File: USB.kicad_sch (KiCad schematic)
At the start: 46 parts, among them J3 USB_C_Receptacle_USB2.0, J4 USB_A_Stacked, U10 TPD4EUSB30, U4 CP2102N-Axx-xQFN20, U5 FSUSB42MUX, U6 FSUSB42MUX, U7 FE1.1, U8 TPD4EUSB30, U9 AP2191W, Y1 12MHz{slash}10pF

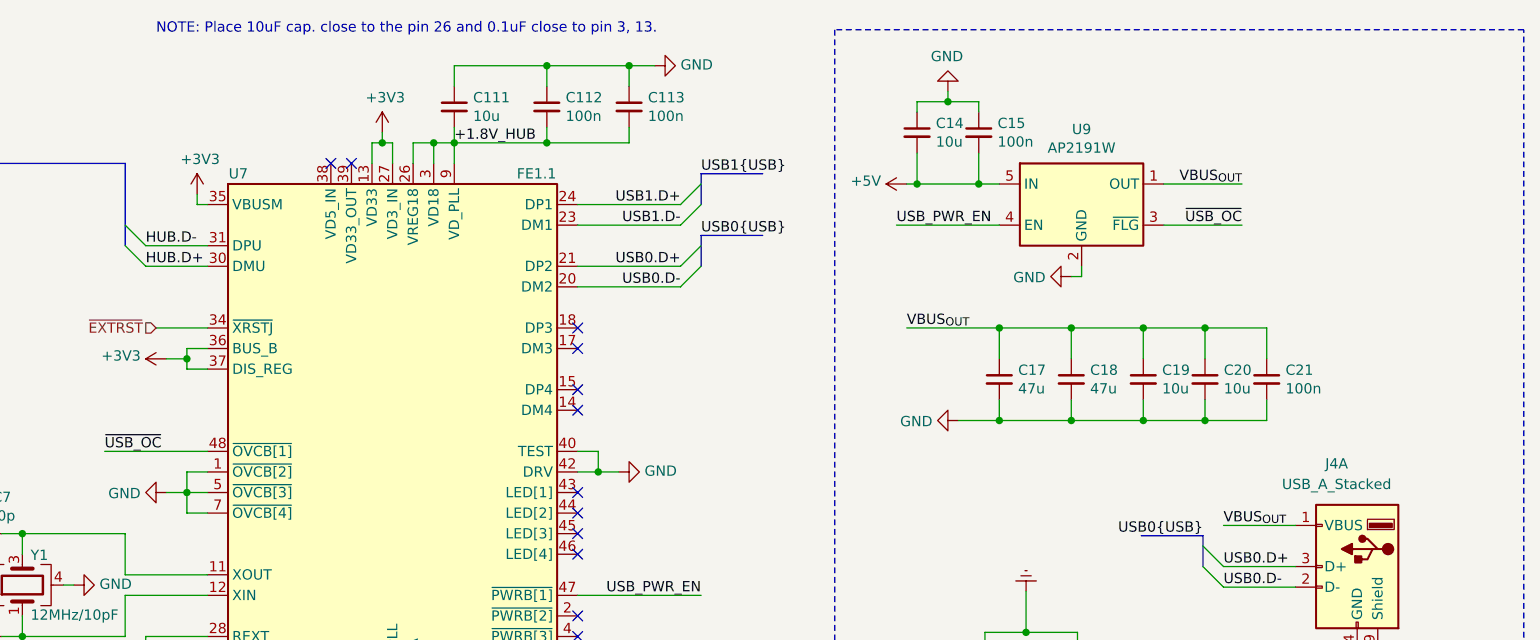
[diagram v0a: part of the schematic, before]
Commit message: USB hub fixes
-Fixed upstream diff pair polarity
-added optional inverer for the USB power switch enable pin
 Design now supports both AP2181 and AP2191

Signed-off-by: Dominik Sliwa <dominik@sliwa.io>
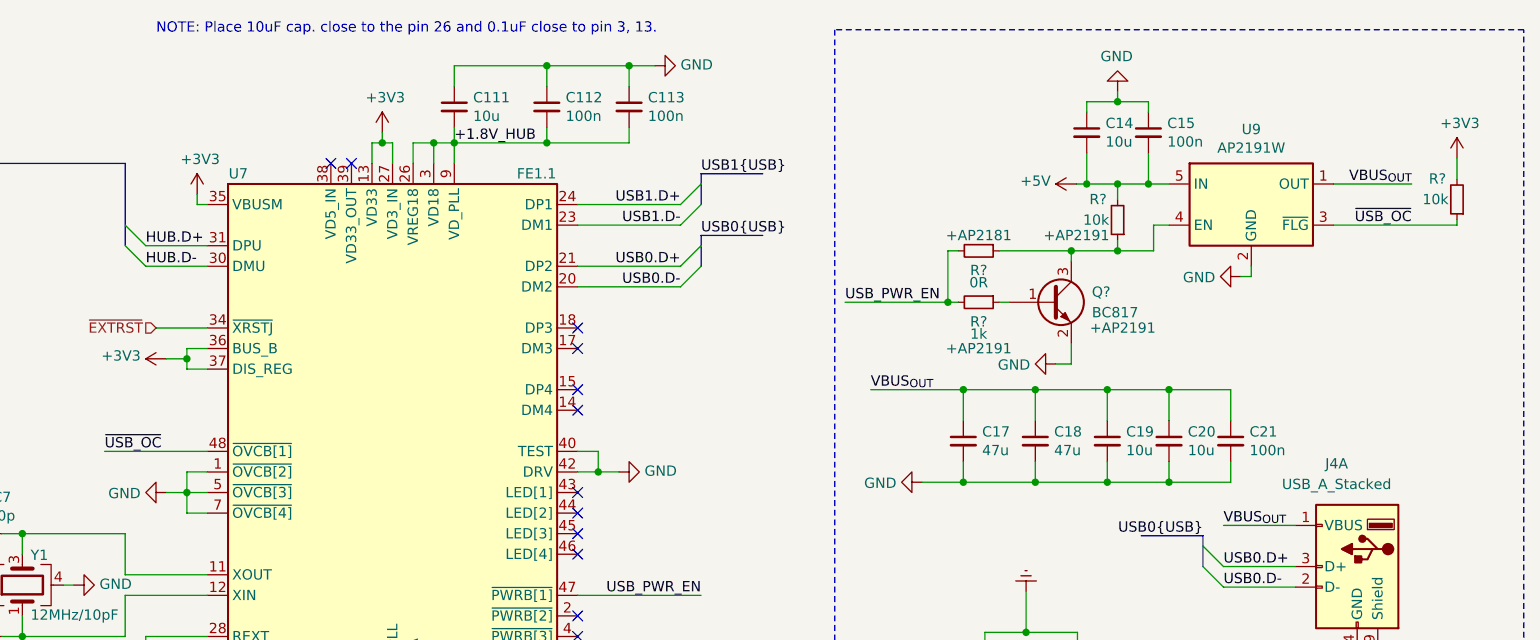
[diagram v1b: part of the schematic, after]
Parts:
- added Q?: BC817, Package_TO_SOT_SMD:SOT-23, symbol Transistor_BJT:BC817
- added R?: 1k, Resistor_SMD:R_0402_1005Metric, symbol Device:R_Small
- added R? (x2): 10k, Resistor_SMD:R_0402_1005Metric, symbol Device:R_Small
- added R?: 0R, Resistor_SMD:R_0402_1005Metric, symbol Device:R_Small
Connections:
- net +3V3: now also R?.2
- net +5V: now also R?.2
- net GND: now also Q?.2 (E)
- net HUB.D+: now also U7.31 (DPU); no longer U7.30 (DMU)
- net HUB.D-: now also U7.30 (DMU); no longer U7.31 (DPU)
- net USB_PWR_EN: now also R?.2, R?.2; no longer U9.4 (EN)
- net ~{USB_OC}: now also R?.1
- new net: Q?.1 (B), R?.1
- new net: Q?.3 (C), R?.1, R?.1, U9.4 (EN)
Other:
- moved on the sheet: C14, C15, C17, C18, C19, C20, C21, U9

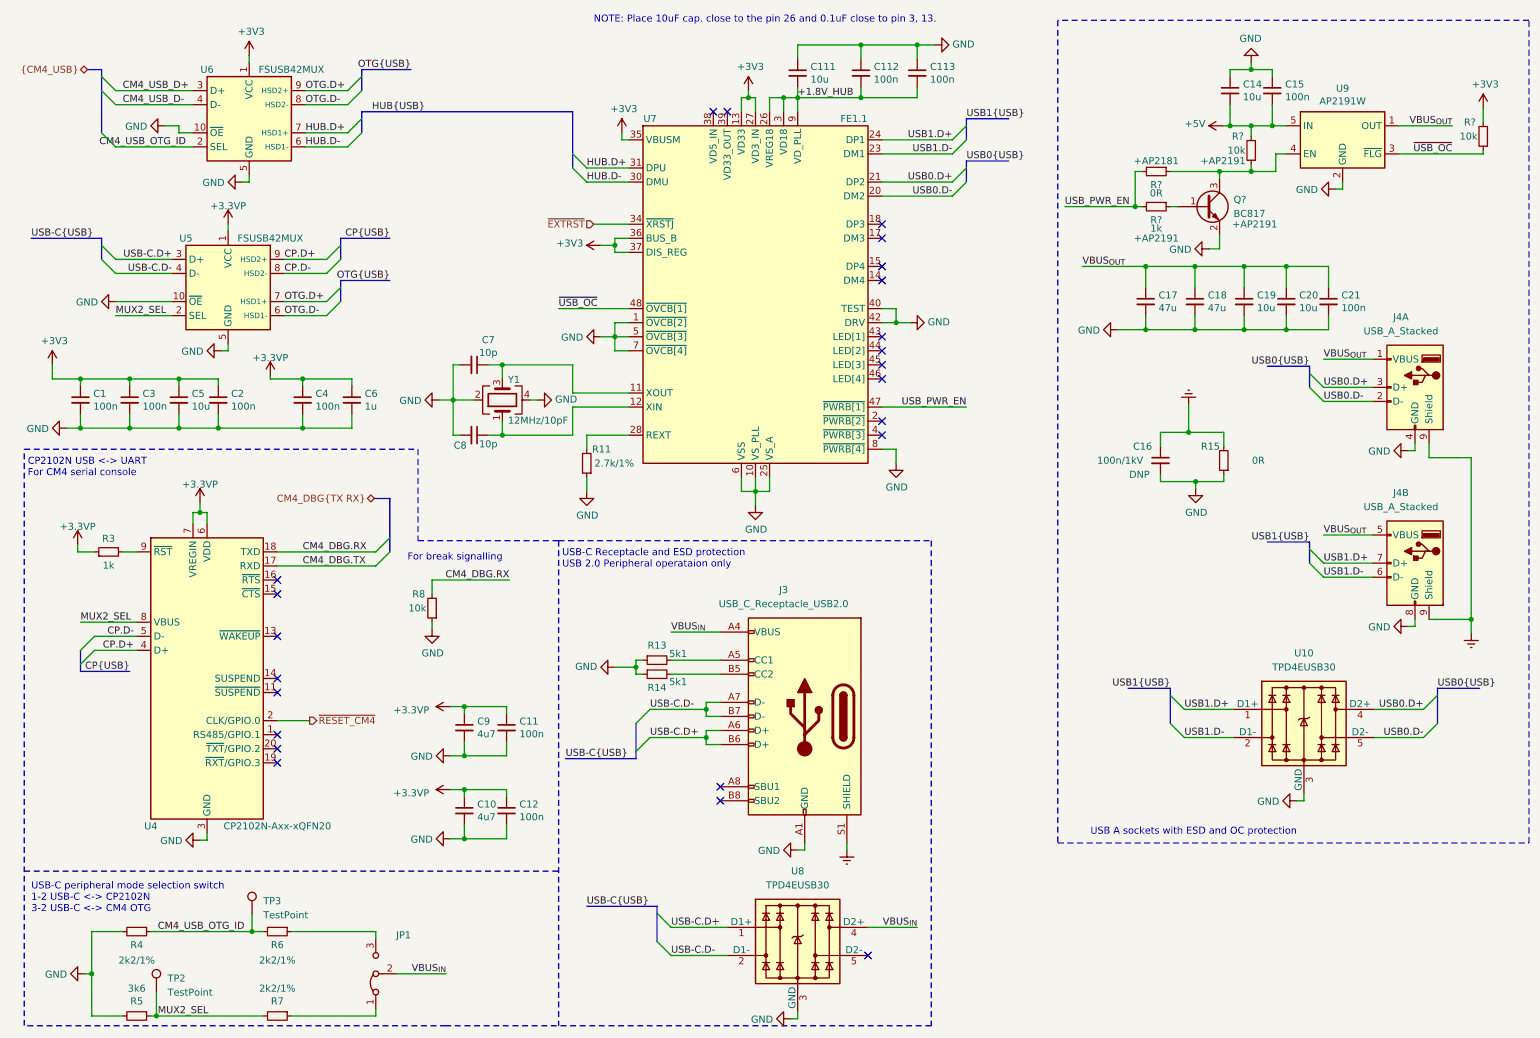
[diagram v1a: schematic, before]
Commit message: Yellow Proto1
Changes:
-name changed to yellow
-moved to 24-pin CP2102N
-routing

Signed-off-by: Dominik Sliwa <dominik@sliwa.io>
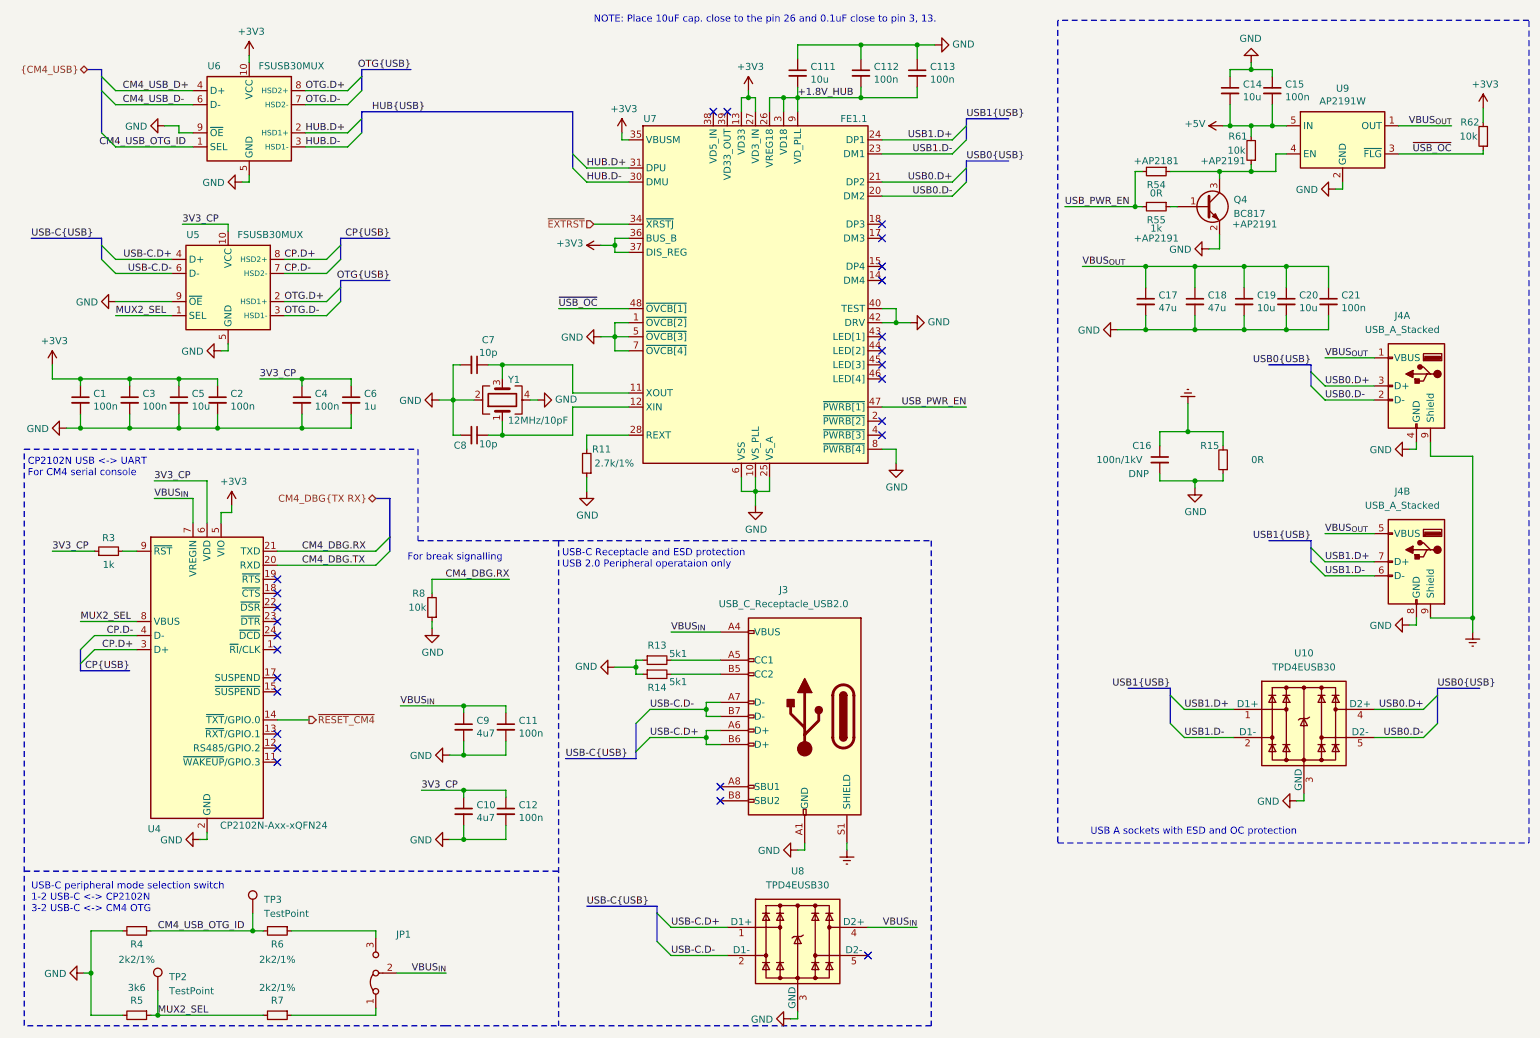
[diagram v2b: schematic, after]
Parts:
- removed U4: CP2102N-Axx-xQFN20, Package_DFN_QFN:SiliconLabs_QFN-20-1EP_3x3mm_P0.5mm_EP1.8x1.8mm, symbol Interface_USB:CP2102N-Axx-xQFN20
- removed U5, U6: FSUSB42MUX, Package_SO:MSOP-10_3x3mm_P0.5mm, symbol Interface_USB:FSUSB42MUX
- added U4: CP2102N-Axx-xQFN24, Package_DFN_QFN:QFN-24-1EP_4x4mm_P0.5mm_EP2.6x2.6mm, symbol Interface_USB:CP2102N-Axx-xQFN24
- added U5, U6: FSUSB30MUX, Package_SO:MSOP-10_3x3mm_P0.5mm, symbol Amber:FSUSB30MUX
- C5: footprint Capacitor_SMD:C_0402_1005Metric -> Capacitor_SMD:C_0805_2012Metric
- gave numbers to parts that had none: 5
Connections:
- net +3V3: now also U4.5 (VIO), U6.10 (VCC)
- net CM4_DBG.RX: now also U4.21 (TXD)
- net CM4_DBG.TX: now also U4.20 (RXD)
- net CM4_USB_D+: now also U6.4 (D+)
- net CM4_USB_D-: now also U6.6 (D-)
- net CM4_USB_OTG_ID: now also U6.1 (SEL)
- net CP.D+: now also U4.3 (D+), U5.8 (HSD2+)
- net CP.D-: now also U4.4 (D-), U5.7 (HSD2-)
- net GND: now also U4.2 (GND), U4.25 (GND), U5.5 (GND), U5.9 (~{OE}), U6.5 (GND), U6.9 (~{OE})
- net HUB.D+: now also U6.2 (HSD1+)
- net HUB.D-: now also U6.3 (HSD1-)
- net MUX2_SEL: now also U4.8 (VBUS), U5.1 (SEL)
- net OTG.D+: now also U5.2 (HSD1+), U6.8 (HSD2+)
- net OTG.D-: now also U5.3 (HSD1-), U6.7 (HSD2-)
- net USB-C.D+: now also U5.4 (D+)
- net USB-C.D-: now also U5.6 (D-)
- net VBUS_{IN}: now also C11.1, C9.1, U4.7 (VREGIN)
- net ~{RESET_CM4}: now also U4.14 (~{TXT}/GPIO.0)
- net at R3.2: now also U4.9 (~{RST})
- net +3.3VP renamed 3V3_CP
- net 3V3_CP: now also U4.6 (VDD), U5.10 (VCC); no longer C11.1, C9.1
- no-connect marks 23 -> 26
